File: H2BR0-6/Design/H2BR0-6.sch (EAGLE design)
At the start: 68 parts, among them J1 SJ-3524-SMT-TRU, J3 440054-3, P2 HEXABIT_X2_P1_P5, U1 STM32G0B1CEU6QFN_B1CEU6_STM-L, U2 AD8232ACPZ-R7, U3 TSV772IQ2T_SEPARATED_SYMBOLSS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, X1 XTALL_CSTCE8M00G52

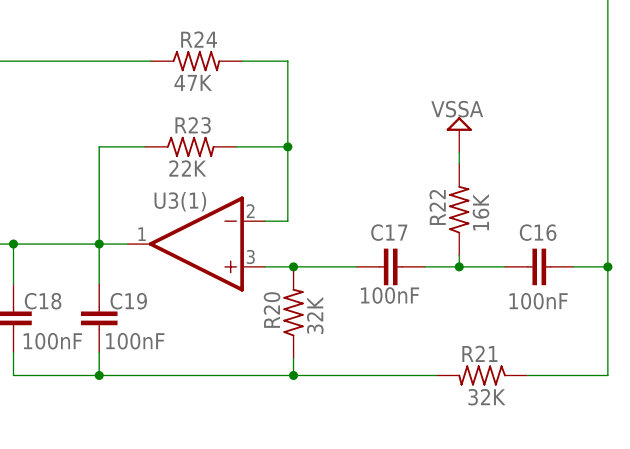
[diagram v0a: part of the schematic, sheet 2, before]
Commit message: Adding the 60Hz version.
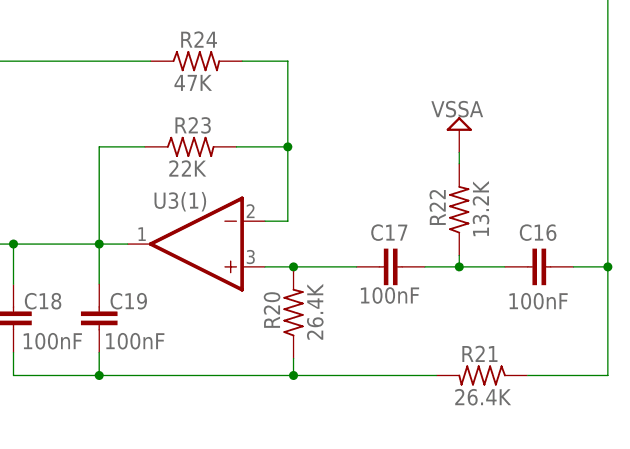
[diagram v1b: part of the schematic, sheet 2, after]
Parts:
- R20, R21: value 32K -> 26.4K
- R22: value 16K -> 13.2K
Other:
- note added: "EXG Monitor (US Version)"
- note added: "H2BR0-6"
- note added: "Notch filter 60Hz Gain = 1.47"
- note removed: "EXG Monitor (EU Version)"
- note removed: "H2BR0-5"
- note removed: "Notch filter 50Hz Gain = 1.47"
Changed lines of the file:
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@@
 <setting verticaltext="up"/>
 </settings>
-<grid distance="0.1" unitdist="inch" unit="inch" style="lines" multiple="1" display="no" altdistance="0.01" altunitdist="inch" altunit="inch"/>
+<grid distance="0.025" unitdist="inch" unit="inch" style="lines" multiple="1" display="no" altdistance="0.01" altunitdist="inch" altunit="inch"/>
 <layers>
 <layer number="1" name="Top" color="4" fill="1" visible="no" active="no"/>
@@
 <part name="R19" library="HEXABITZ_RCLS" library_urn="urn:adsk.eagle:library:20064561" deviceset="R-0402" device="" package3d_urn="urn:adsk.eagle:package:19666455/4" value="200K"/>
 <part name="C15" library="HEXABITZ_RCLS" library_urn="urn:adsk.eagle:library:20064561" deviceset="C-0402" device="" package3d_urn="urn:adsk.eagle:package:19666459/4" value="100nF"/>
-<part name="R20" library="HEXABITZ_RCLS" library_urn="urn:adsk.eagle:library:20064561" deviceset="R-0402" device="" package3d_urn="urn:adsk.eagle:package:19666455/4" value="32K"/>
-<part name="R21" library="HEXABITZ_RCLS" library_urn="urn:adsk.eagle:library:20064561" deviceset="R-0402" device="" package3d_urn="urn:adsk.eagle:package:19666455/4" value="32K"/>
+<part name="R20" library="HEXABITZ_RCLS" library_urn="urn:adsk.eagle:library:20064561" deviceset="R-0402" device="" package3d_urn="urn:adsk.eagle:package:19666455/4" value="26.4K"/>
+<part name="R21" library="HEXABITZ_RCLS" library_urn="urn:adsk.eagle:library:20064561" deviceset="R-0402" device="" package3d_urn="urn:adsk.eagle:package:19666455/4" value="26.4K"/>
 <part name="C16" library="HEXABITZ_RCLS" library_urn="urn:adsk.eagle:library:20064561" deviceset="C-0402" device="" package3d_urn="urn:adsk.eagle:package:19666459/4" value="100nF"/>
 <part name="C17" library="HEXABITZ_RCLS" library_urn="urn:adsk.eagle:library:20064561" deviceset="C-0402" device="" package3d_urn="urn:adsk.eagle:package:19666459/4" value="100nF"/>
 <part name="C18" library="HEXABITZ_RCLS" library_urn="urn:adsk.eagle:library:20064561" deviceset="C-0402" device="" package3d_urn="urn:adsk.eagle:package:19666459/4" value="100nF"/>
-<part name="R22" library="HEXABITZ_RCLS" library_urn="urn:adsk.eagle:library:20064561" deviceset="R-0402" device="" package3d_urn="urn:adsk.eagle:package:19666455/4" value="16K"/>
+<part name="R22" library="HEXABITZ_RCLS" library_urn="urn:adsk.eagle:library:20064561" deviceset="R-0402" device="" package3d_urn="urn:adsk.eagle:package:19666455/4" value="13.2K"/>
 <part name="R23" library="HEXABITZ_RCLS" library_urn="urn:adsk.eagle:library:20064561" deviceset="R-0402" device="" package3d_urn="urn:adsk.eagle:package:19666455/4" value="22K"/>
 <part name="R24" library="HEXABITZ_RCLS" library_urn="urn:adsk.eagle:library:20064561" deviceset="R-0402" device="" package3d_urn="urn:adsk.eagle:package:19666455/4" value="47K"/>
@@
 <text x="216.45" y="4.9548" size="1.9304" layer="100" font="vector">Sheet   of</text>
 <text x="200.0162" y="19.2042" size="1.9304" layer="100" font="vector">Title</text>
-<text x="181.4742" y="19.2042" size="1.9304" layer="102" font="vector">H2BR0-5</text>
-<text x="177.2578" y="10.7714" size="1.9304" layer="101" font="vector">EXG Monitor (EU Version)</text>
+<text x="181.4742" y="19.2042" size="1.9304" layer="102" font="vector">H2BR0-6</text>
+<text x="177.2578" y="10.7714" size="1.9304" layer="101" font="vector">EXG Monitor (US Version)</text>
 <text x="206.8742" y="19.2042" size="1.9304" layer="101" font="vector">H2BR0_Backend</text>
 <wire x1="169.46" y1="3.38" x2="169.46" y2="7.698" width="0.1524" layer="205"/>
@@
 <text x="216.45" y="4.9548" size="1.9304" layer="100" font="vector">Sheet   of</text>
 <text x="200.0162" y="19.2042" size="1.9304" layer="100" font="vector">Title</text>
-<text x="181.4742" y="19.2042" size="1.9304" layer="102" font="vector">H2BR0-5</text>
-<text x="177.2578" y="10.7714" size="1.9304" layer="101" font="vector">EXG Monitor (EU Version)</text>
+<text x="181.4742" y="19.2042" size="1.9304" layer="102" font="vector">H2BR0-6</text>
+<text x="177.2578" y="10.7714" size="1.9304" layer="101" font="vector">EXG Monitor (US Version)</text>
 <text x="206.8742" y="19.2042" size="1.9304" layer="101" font="vector">H2BR0_Frontend</text>
 <wire x1="169.46" y1="3.38" x2="169.46" y2="7.698" width="0.1524" layer="205"/>
@@
 <wire x1="151.765" y1="40.64" x2="151.765" y2="88.9" width="0.1524" layer="101"/>
 <wire x1="151.765" y1="88.9" x2="185.42" y2="88.9" width="0.1524" layer="101"/>
-<text x="217.805" y="31.75" size="2.54" layer="100">Notch filter 50Hz
+<text x="217.805" y="31.75" size="2.54" layer="100">Notch filter 60Hz
     Gain = 1.47</text>
 <wire x1="106.68" y1="88.9" x2="106.68" y2="40.64" width="0.1524" layer="101"/>
@@
 <instance part="R20" gate="G$1" x="228.6" y="55.245" smashed="yes" rot="R90">
 <attribute name="NAME" x="227.1014" y="53.34" size="1.778" layer="95" rot="R90"/>
-<attribute name="VALUE" x="231.902" y="52.705" size="1.778" layer="96" rot="R90"/>
+<attribute name="VALUE" x="231.902" y="52.07" size="1.778" layer="96" rot="R90"/>
 </instance>
 <instance part="R21" gate="G$1" x="249.555" y="48.26" smashed="yes" rot="MR0">
 <attribute name="NAME" x="251.46" y="49.7586" size="1.778" layer="95" rot="MR0"/>
-<attribute name="VALUE" x="252.095" y="44.958" size="1.778" layer="96" rot="MR0"/>
+<attribute name="VALUE" x="252.73" y="44.958" size="1.778" layer="96" rot="MR0"/>
 </instance>
 <instance part="C16" gate="G$1" x="257.175" y="60.325" smashed="yes" rot="MR270">
@@
 <instance part="R22" gate="G$1" x="247.015" y="66.675" smashed="yes" rot="R90">
 <attribute name="NAME" x="245.5164" y="64.77" size="1.778" layer="95" rot="R90"/>
-<attribute name="VALUE" x="250.317" y="64.135" size="1.778" layer="96" rot="R90"/>
+<attribute name="VALUE" x="250.317" y="63.5" size="1.778" layer="96" rot="R90"/>
 </instance>
 <instance part="R23" gate="G$1" x="217.17" y="73.66" smashed="yes">
